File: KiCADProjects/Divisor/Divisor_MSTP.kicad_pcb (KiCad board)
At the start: 2 copper layers, 94.2 x 94.6 mm, 34 parts, among them J1 SMA_Female, J10 SMA_Female, J11 SMA_Female, J12 SMA_Female, J13 SMA_Female, J14 SMA_Female, J15 SMA_Female, J16 SMA_Female, J17 SMA_Female, J2 SMA_Female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

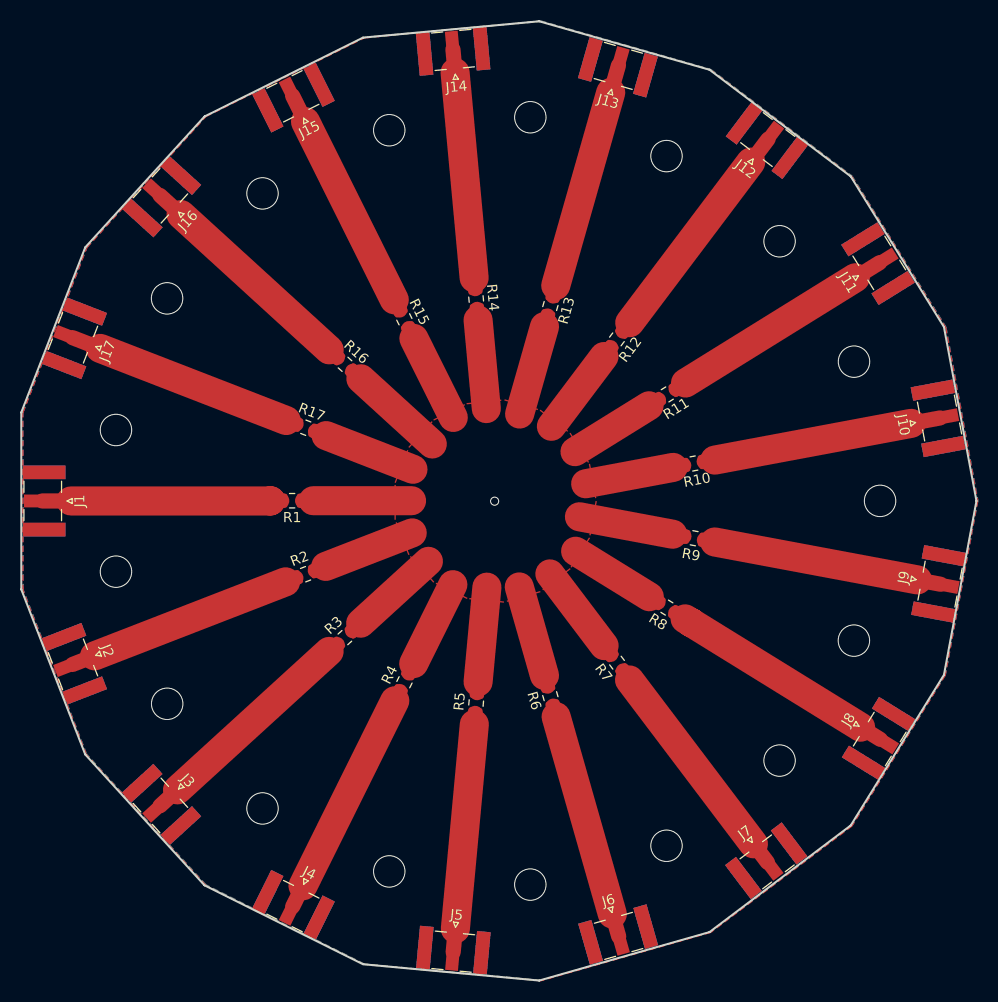
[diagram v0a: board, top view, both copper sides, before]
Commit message: MSTP no tiene plano de tierra!
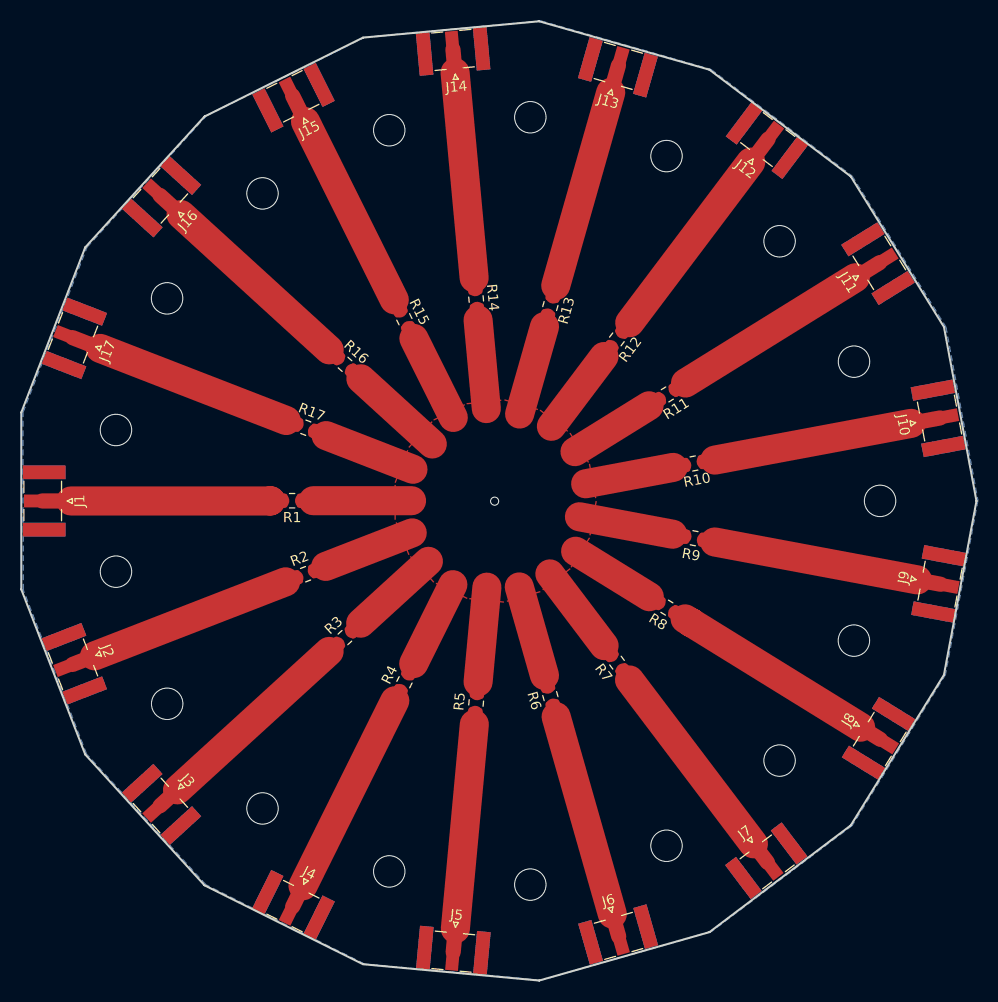
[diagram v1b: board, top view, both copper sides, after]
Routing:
- removed copper zone on F.Cu, net GND
